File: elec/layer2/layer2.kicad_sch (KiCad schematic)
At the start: 0 parts

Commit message: feat: layer2 motor driver footprint and schematic
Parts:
- added U1: ~, layer2-pcb-footprints:buck-module, symbol layer2-pcb-symbols:buck-module
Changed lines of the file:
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@@
 	(generator_version "9.0")
 	(paper "A4")
+	(symbol
+		(lib_id "layer2-pcb-symbols:buck-module")
+		(at 109.22 101.6 0)
+		(unit 1)
+		(exclude_from_sim no)
+		(in_bom yes)
+		(on_board yes)
+		(dnp no)
+		(fields_autoplaced yes)
+		(property "Reference" "U1"
+			(at 109.22 90.17 0)
+			(effects
+				(font
+					(size 1.27 1.27)
+				)
+			)
+		)
+		(property "Value" "~"
+			(at 109.22 92.71 0)
+			(effects
+				(font
+					(size 1.27 1.27)
+				)
+			)
+		)
+		(property "Footprint" "layer2-pcb-footprints:buck-module"
+			(at 109.22 116.84 0)
+			(effects
+				(font
+					(size 1.27 1.27)
+				)
+				(hide yes)
+			)
+		)
+		(property "Datasheet" ""
+			(at 109.22 101.6 0)
+			(effects
+				(font
+					(size 1.27 1.27)
+				)
+				(hide yes)
+			)
+		)
+		(property "Description" ""
+			(at 109.22 101.6 0)
+			(effects
+				(font
+					(size 1.27 1.27)
+				)
+				(hide yes)
+			)
+		)
+		(pin "1"
+		)
+		(pin "4"
+		)
+		(pin "3"
+		)
+		(pin "2"
+		)
+		(instances
+			(project ""
+				(path "/3575a11a-9f0c-4991-9971-4ac931abf689"
+					(reference "U1")
+					(unit 1)
+				)
+			)
+		)
+	)
 	(sheet_instances
 		(path "/"

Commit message: feat: did something
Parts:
- added H1, H10, H11, H12, H2, H3, H4, H5, H6, H7, H8, H9: MountingHole, MountingHole:MountingHole_3.2mm_M3_DIN965_Pad, symbol Mechanical:MountingHole
- added U2, U3, U4, U5: ~, layer2-pcb-footprints:motor-driver-module, symbol layer2-pcb-symbols:motor-driver-module
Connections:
- net GND: now reaches U1.2 (GND)
- net GND: now also U2.7 (GND), U3.7 (GND), U4.7 (GND), U5.7 (GND)

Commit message: did smth
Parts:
- added BatteryConnection1, KillSwitch1: Conn_01x02, layer2-pcb-footprints:AMASS_XT60-M, symbol Connector_Generic:Conn_01x02
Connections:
- net GND: now also BatteryConnection1.1 (Pin_1), KillSwitch1.1 (Pin_1)
- new net +12V: BatteryConnection1.2 (Pin_2), KillSwitch1.2 (Pin_2)

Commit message: did some stuff on l2
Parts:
- removed BatteryConnection1: Conn_01x02, layer2-pcb-footprints:AMASS_XT60-M, symbol Connector_Generic:Conn_01x02
- removed U4, U5: ~, layer2-pcb-footprints:motor-driver-module, symbol layer2-pcb-symbols:motor-driver-module
- added DribblerConnection1: Conn_01x03, Pinheaders:PinHeader_1x03_P2.54mm_Vertical, symbol Connector_Generic:Conn_01x03
- added DribblerConnection2: Conn_01x02, Connector_AMASS:AMASS_XT30U-F_1x02_P5.0mm_Vertical, symbol Connector_Generic:Conn_01x02
- added KillSwitch: SW_SPST, Connector_AMASS:AMASS_XT30PW-M_1x02_P2.50mm_Horizontal, symbol Switch:SW_SPST
- added L1-->L2Connection1, L1-->L2Connection2, L2-->L3Connection1, L2-->L3Connection2: Conn_01x08, Pinheaders:PinHeader_1x08_P2.54mm_Vertical, symbol Connector_Generic:Conn_01x08
- added Lightgate(LDR)1, Lightgate(LED)1: Conn_01x02, Connector_JST:JST_SH_BM02B-SRSS-TB_1x02-1MP_P1.00mm_Vertical, symbol Connector_Generic:Conn_01x02
- added U4: DEV-15583, layer2-pcb-footprints:MODULE_DEV-15583, symbol Teensy4.0:DEV-15583
- KillSwitch1: footprint layer2-pcb-footprints:AMASS_XT60-M -> Connector_AMASS:AMASS_XT30U-F_1x02_P5.0mm_Vertical
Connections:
- net +12V: now also U1.1 (12v), U2.1 (12v), U3.1 (12v), DribblerConnection2.1 (Pin_1), KillSwitch.1 (A), L1-->L2Connection2.1 (Pin_1), L1-->L2Connection2.2 (Pin_2), L1-->L2Connection2.3 (Pin_3), L2-->L3Connection1.1 (Pin_1), L2-->L3Connection1.2 (Pin_2), L2-->L3Connection1.3 (Pin_3); no longer KillSwitch1.2 (Pin_2)
- net GND: now also DribblerConnection1.3 (Pin_3), DribblerConnection2.2 (Pin_2), L1-->L2Connection1.7 (Pin_7), L1-->L2Connection1.8 (Pin_8), L1-->L2Connection2.6 (Pin_6), L1-->L2Connection2.7 (Pin_7), L1-->L2Connection2.8 (Pin_8), L2-->L3Connection1.6 (Pin_6), L2-->L3Connection1.7 (Pin_7), L2-->L3Connection1.8 (Pin_8), L2-->L3Connection2.7 (Pin_7), L2-->L3Connection2.8 (Pin_8), Lightgate(LED)1.1 (Pin_1), U4.G1, U4.G2, U4.G3
- net +3V3: now reaches U1.3 (3v3)
- net +3V3: now also U2.2 (3v3), U3.2 (3v3), DribblerConnection1.1 (Pin_1), L1-->L2Connection1.1 (Pin_1), L1-->L2Connection1.2 (Pin_2), L1-->L2Connection1.3 (Pin_3), L2-->L3Connection2.1 (Pin_1), L2-->L3Connection2.2 (Pin_2), L2-->L3Connection2.3 (Pin_3), Lightgate(LDR)1.2 (Pin_2), Lightgate(LED)1.2 (Pin_2), U4.3.3V_1, U4.3.3V_2
- net +5V: now reaches U1.4 (5v)
- net +5V: now also L1-->L2Connection1.4 (Pin_4), L1-->L2Connection1.5 (Pin_5), L2-->L3Connection2.4 (Pin_4), L2-->L3Connection2.5 (Pin_5), U4.VIN
- net M SW: now reaches U3.3 (EN)
- net M SW: now also U2.3 (EN), L1-->L2Connection1.6 (Pin_6), L2-->L3Connection2.6 (Pin_6)
- net M4 IN A: now reaches U3.4 (MOTOR_IN_A)
- net M4 IN A: now also U4.18
- net M4 IN B: now reaches U3.5 (MOTOR_IN_B)
- net M4 IN B: now also U4.19
- net M4 PWM: now reaches U3.6 (MOTOR_PWM)
- net M4 PWM: now also U4.20
- net M3 IN A: now reaches U2.4 (MOTOR_IN_A)
- net M3 IN A: now also U4.21
- net M3 IN B: now reaches U2.5 (MOTOR_IN_B)
- net M3 IN B: now also U4.22
- net M3 PWM: now reaches U2.6 (MOTOR_PWM)
- net M3 PWM: now also U4.23
- new net: KillSwitch.2 (B), KillSwitch1.2 (Pin_2)
- new net Dribbler Data: DribblerConnection1.2 (Pin_2), U4.17
- new net LightGateLDR: Lightgate(LDR)1.1 (Pin_1), U4.16
- new net RX: L1-->L2Connection2.4 (Pin_4), L2-->L3Connection1.4 (Pin_4)
- new net TX: L1-->L2Connection2.5 (Pin_5), L2-->L3Connection1.5 (Pin_5)
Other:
- note added: "Connections"
- note added: "Modules"
- note added: "Mounting Holes"
- moved on the sheet: H1, H10, H11, H12, H2, H3, H4, H5, H6, H7, H8, H9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

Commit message: did something
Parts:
- KillSwitch2: renamed from KillSwitch; footprint Connector_AMASS:AMASS_XT30PW-M_1x02_P2.50mm_Horizontal -> Connector_AMASS:AMASS_XT30U-F_1x02_P5.0mm_Vertical
- renumbered KillSwitch1 to BatteryConnection1
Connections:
- net Dribbler Data: now also U4.3; no longer U4.17
- net LightGateLDR: now also U4.2; no longer U4.16
- net M3 IN A: now also U4.4; no longer U4.21
- net M3 IN B: now also U4.5; no longer U4.22
- net M3 PWM: now also U4.6; no longer U4.23
- net M4 IN A: now also U4.7; no longer U4.18
- net M4 IN B: now also U4.8; no longer U4.19
- net M4 PWM: now also U4.9; no longer U4.20
- net RX: now also L1-->L2Connection2.5 (Pin_5), U4.0; no longer L1-->L2Connection2.4 (Pin_4)
- net TX: now also L1-->L2Connection2.4 (Pin_4), U4.1; no longer L1-->L2Connection2.5 (Pin_5)
- no-connect marks 0 -> 17
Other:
- note added: "Dribbler Connections"
- note added: "Inter-layer Connections"
- note added: "Misc.Connections"
- note removed: "Connections"
- moved on the sheet: BatteryConnection1, DribblerConnection1, DribblerConnection2, KillSwitch2, Lightgate(LDR)1, Lightgate(LED)1

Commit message: did smnth to l2
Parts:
- removed L2-->L3Connection1, L2-->L3Connection2: Conn_01x08, Pinheaders:PinHeader_1x08_P2.54mm_Vertical, symbol Connector_Generic:Conn_01x08

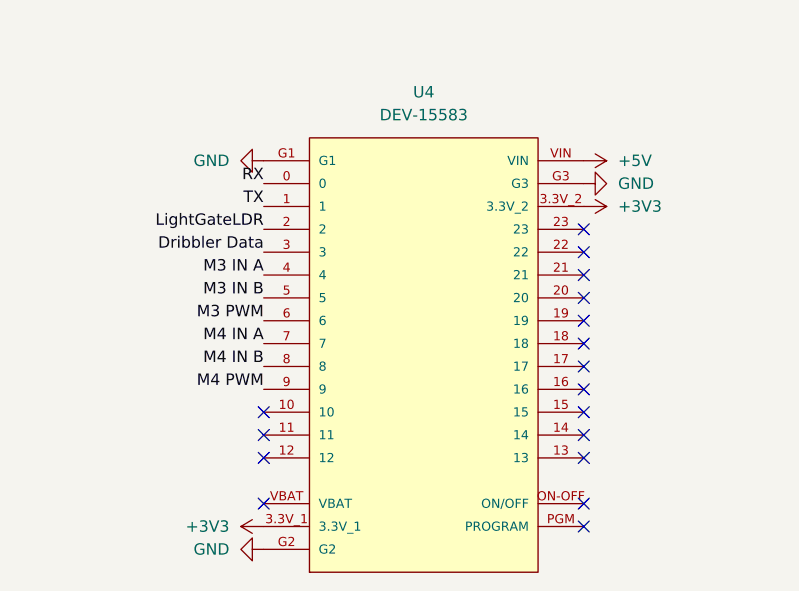
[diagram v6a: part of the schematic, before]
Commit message: FInished L2-l3 connection and branding
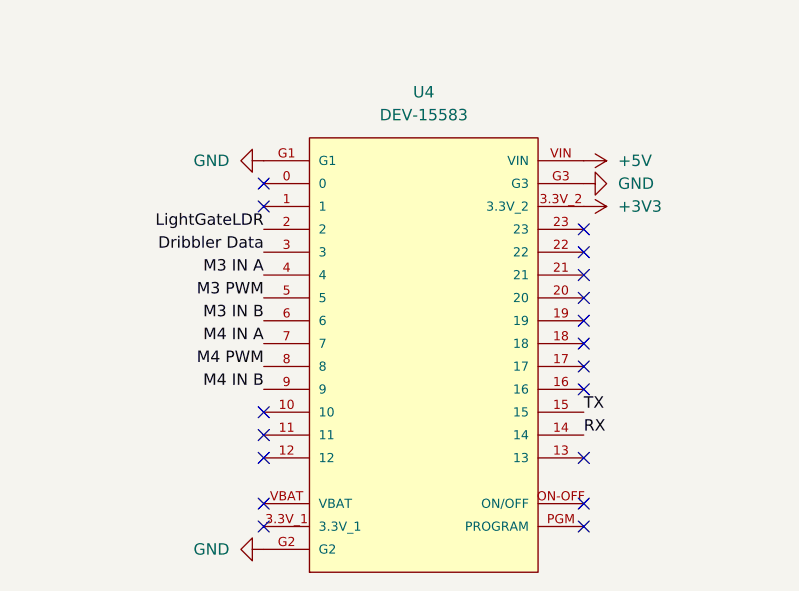
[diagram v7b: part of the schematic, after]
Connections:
- net +3V3: no longer U4.3.3V_1
- net M3 IN B: now also U4.6; no longer U4.5
- net M3 PWM: now also U4.5; no longer U4.6
- net M4 IN B: now also U4.9; no longer U4.8
- net M4 PWM: now also U4.8; no longer U4.9
- net RX: now also U4.14; no longer U4.0
- net TX: now also U4.15; no longer U4.1
- no-connect marks 17 -> 18
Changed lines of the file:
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@@
-	)
-	(no_connect
-		(at 74.93 161.29)
-	)
-	(no_connect
-		(at 74.93 158.75)
 	)
 	(no_connect
@@
 	)
 	(no_connect
+		(at 39.37 135.89)
+	)
+	(no_connect
 		(at 74.93 143.51)
 	)
@@
 	)
 	(no_connect
+		(at 39.37 171.45)
+	)
+	(no_connect
 		(at 74.93 171.45)
+	)
+	(no_connect
+		(at 39.37 133.35)
 	)
 	(no_connect
@@
 	)
 	(label "RX"
-		(at 39.37 133.35 180)
+		(at 74.93 161.29 0)
 		(effects
 			(font
 				(size 1.27 1.27)
 			)
-			(justify right bottom)
+			(justify left bottom)
 		)
 	)
@@
 	)
 	(label "M4 IN B"
-		(at 39.37 153.67 180)
+		(at 39.37 156.21 180)
 		(effects
 			(font
@@
 	)
 	(label "M4 PWM"
-		(at 39.37 156.21 180)
+		(at 39.37 153.67 180)
 		(effects
 			(font
@@
 	)
 	(label "M3 PWM"
-		(at 39.37 148.59 180)
+		(at 39.37 146.05 180)
 		(effects
 			(font
@@
 	)
 	(label "M3 IN B"
-		(at 39.37 146.05 180)
+		(at 39.37 148.59 180)
 		(effects
 			(font
@@
 	)
 	(label "TX"
-		(at 39.37 135.89 180)
+		(at 74.93 158.75 0)
 		(effects
 			(font
 				(size 1.27 1.27)
 			)
-			(justify right bottom)
+			(justify left bottom)
 		)
 	)
@@
 					(unit 1)
 				)
-			)
-		)
-	)
-	(symbol
-		(lib_id "power:+3V3")
-		(at 39.37 171.45 90)
-		(unit 1)
-		(exclude_from_sim no)
-		(in_bom yes)
-		(on_board yes)
-		(dnp no)
-		(fields_autoplaced yes)
-		(property "Reference" "#PWR029"
-			(at 43.18 171.45 0)
-			(effects
-				(font
-					(size 1.27 1.27)
-				)
-				(hide yes)
-			)
-		)
-		(property "Value" "+3V3"
-			(at 35.56 171.4499 90)
-			(effects
-				(font
-					(size 1.27 1.27)
-				)
-				(justify left)
-			)
-		)
-		(property "Footprint" ""
-			(at 39.37 171.45 0)
-			(effects
-				(font
-					(size 1.27 1.27)
-				)
-				(hide yes)
-			)
-		)
-		(property "Datasheet" ""
-			(at 39.37 171.45 0)
-			(effects
-				(font
-					(size 1.27 1.27)
-				)
-				(hide yes)
-			)
-		)
-		(property "Description" "Power symbol creates a global label with name \"+3V3\""
-			(at 39.37 171.45 0)
-			(effects
-				(font
-					(size 1.27 1.27)
-				)
-				(hide yes)
-			)
-		)
-		(pin "1"
-		)
-		(instances
-			(project ""
-				(path "/3575a11a-9f0c-4991-9971-4ac931abf689"
-					(reference "#PWR029")
-					(unit 1)
-				)

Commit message: stuff
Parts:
- added J1, J2, L2-->L3Connection1: Conn_01x08, Pinheaders:PinHeader_1x08_P2.54mm_Vertical, symbol Connector_Generic:Conn_01x08
- added J3, J4: Conn_01x08, Connector_PinSocket_2.54mm:PinSocket_1x08_P2.54mm_Vertical, symbol Connector_Generic:Conn_01x08
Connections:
- net +12V: now also J1.1 (Pin_1), J1.2 (Pin_2), J1.3 (Pin_3), J3.1 (Pin_1), J3.2 (Pin_2), J3.3 (Pin_3)
- net +3V3: now also L2-->L3Connection1.8 (Pin_8)
- net +5V: now also L2-->L3Connection1.1 (Pin_1), L2-->L3Connection1.2 (Pin_2)
- net GND: now also J1.6 (Pin_6), J1.7 (Pin_7), J1.8 (Pin_8), J3.6 (Pin_6), J3.7 (Pin_7), J3.8 (Pin_8), J4.6 (Pin_6), J4.7 (Pin_7), J4.8 (Pin_8), L2-->L3Connection1.6 (Pin_6), L2-->L3Connection1.7 (Pin_7)
- net M SW: now also L2-->L3Connection1.3 (Pin_3)
- net RX: now also L2-->L3Connection1.5 (Pin_5)
- net TX: now also L2-->L3Connection1.4 (Pin_4)
- new net +24V: J2.3 (Pin_3), J2.4 (Pin_4), J2.5 (Pin_5), J2.6 (Pin_6), J4.1 (Pin_1), J4.2 (Pin_2), J4.3 (Pin_3), J4.4 (Pin_4)
- new net Sol: J3.4 (Pin_4), J3.5 (Pin_5)
- no-connect marks 18 -> 25
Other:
- moved on the sheet: DribblerConnection1, DribblerConnection2
